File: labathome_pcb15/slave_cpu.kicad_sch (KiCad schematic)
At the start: 47 parts, among them J1 HALL, J26 STDC14, J27 ADDA, J28 Brushless, J30 Servo4, J31 Servo1, J32 Servo2, J33 Servo3, J34 STM32 EXT, U16 LM358, U3 DRV8313, U5 STM32G431R8Tx

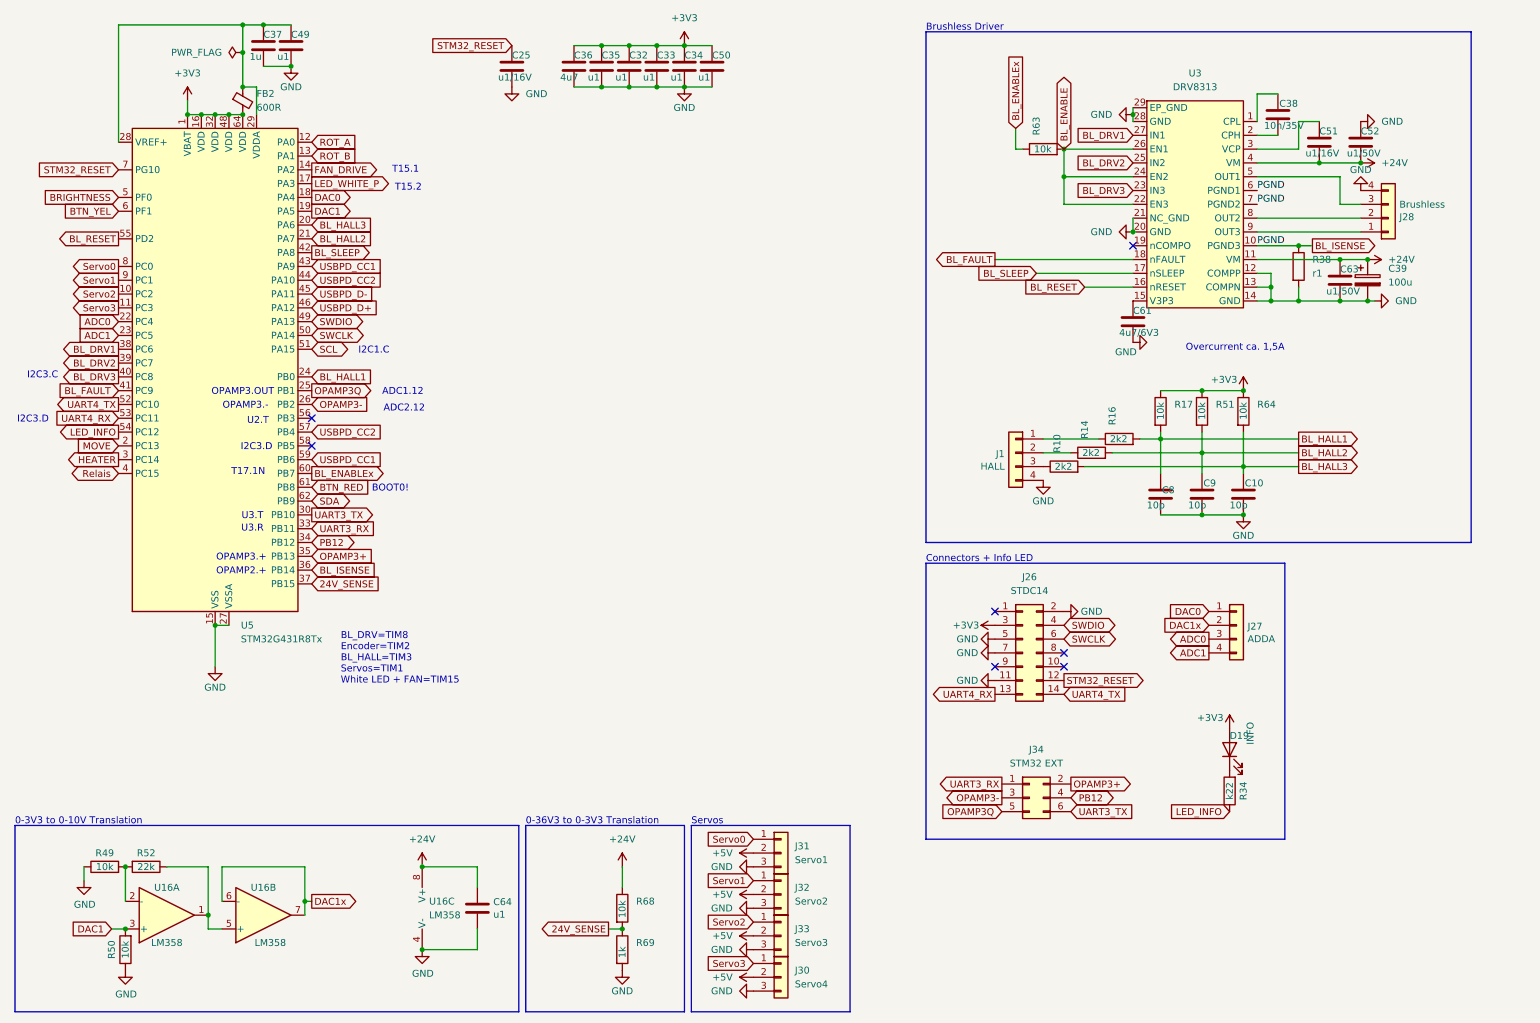
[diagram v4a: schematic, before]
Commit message: Reverse mount LEDs, switch
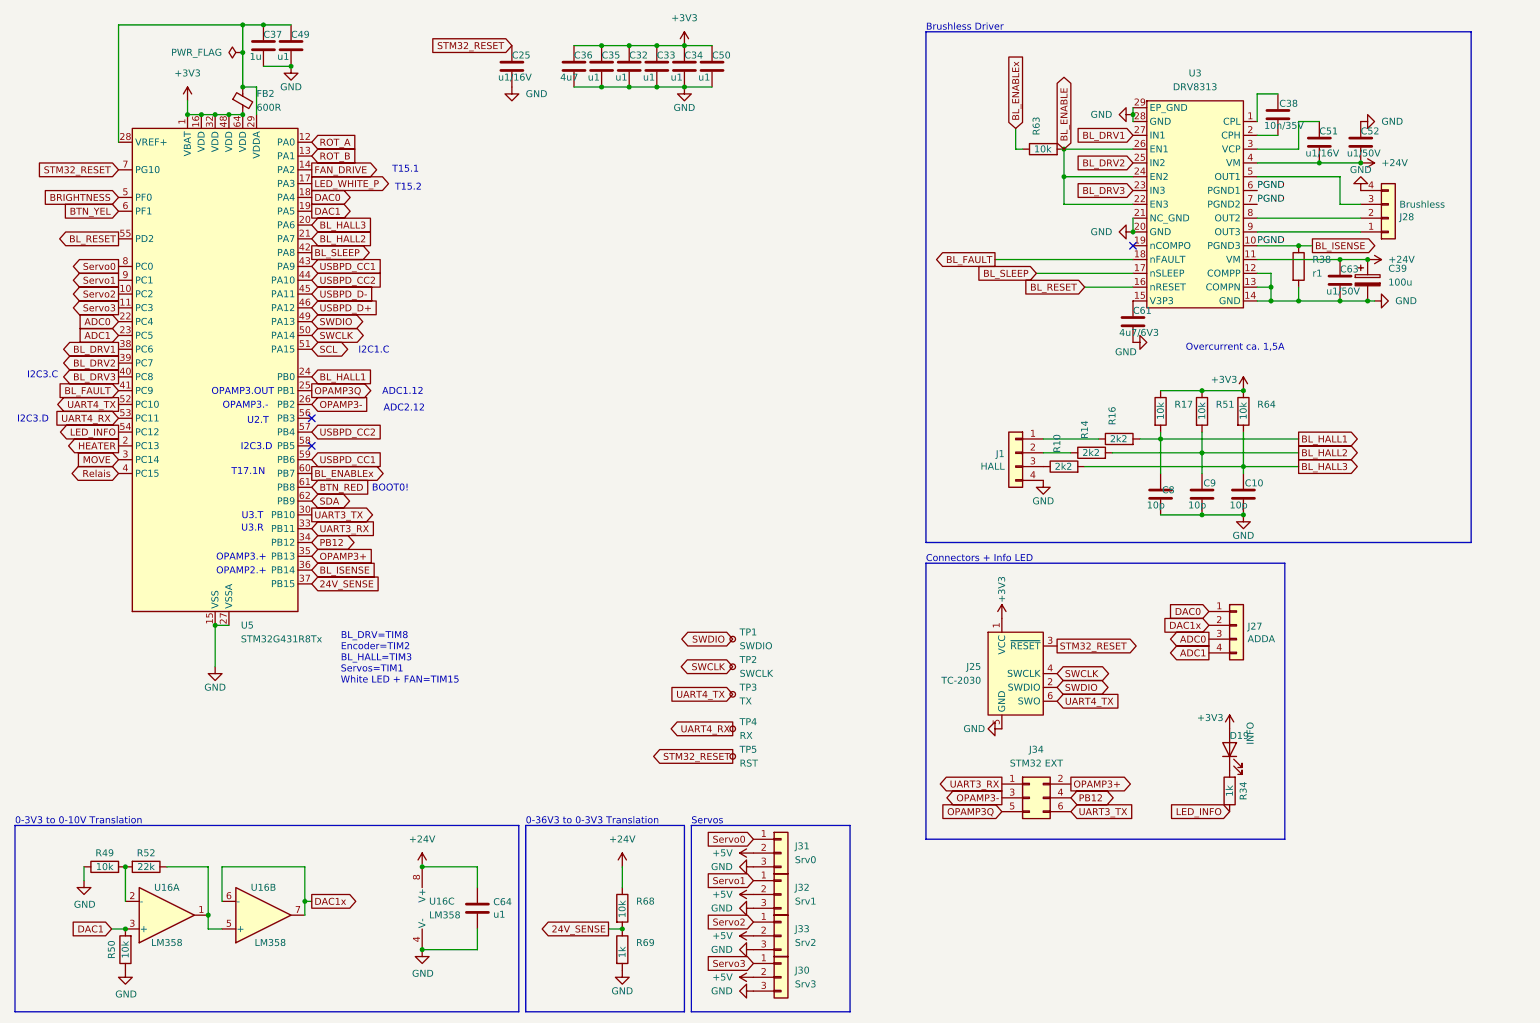
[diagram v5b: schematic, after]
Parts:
- removed J26: STDC14, Connector_IDC:IDC-Header_2x07_P2.54mm_Vertical, symbol Connector_Generic:Conn_02x07_Odd_Even
- added J25: TC-2030, Connector:Tag-Connect_TC2030-IDC-NL_2x03_P1.27mm_Vertical, symbol Connector:Conn_ARM_SWD_TagConnect_TC2030-NL
- added TP1: SWDIO, TestPoint:TestPoint_THTPad_D1.5mm_Drill0.7mm, symbol Connector:TestPoint_Small
- added TP2: SWCLK, TestPoint:TestPoint_THTPad_D1.5mm_Drill0.7mm, symbol Connector:TestPoint_Small
- added TP3: TX, TestPoint:TestPoint_THTPad_D1.5mm_Drill0.7mm, symbol Connector:TestPoint_Small
- added TP4: RX, TestPoint:TestPoint_THTPad_D1.5mm_Drill0.7mm, symbol Connector:TestPoint_Small
- added TP5: RST, TestPoint:TestPoint_THTPad_D1.5mm_Drill0.7mm, symbol Connector:TestPoint_Small
- D19: footprint LED_SMD:LED_0805_2012Metric_Pad1.15x1.40mm_HandSolder -> liebler_OPTO:LED_1206_3216Metric_ReverseMount
- J30: value Servo4 -> Srv3
- J31: value Servo1 -> Srv0
- J32: value Servo2 -> Srv1
- J33: value Servo3 -> Srv2
- R34: value k22 -> 1k
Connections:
- net +3V3: now also J25.1 (VCC)
- net GND: now also J25.5 (GND)
- net HEATER: now also U5.2 (PC13); no longer U5.3 (PC14)
- net MOVE: now also U5.3 (PC14); no longer U5.2 (PC13)
- net STM32_RESET: now also J25.3 (~{RESET}), TP5.1
- net SWCLK: now also J25.4 (SWCLK), TP2.1
- net SWDIO: now also J25.2 (SWDIO), TP1.1
- net UART4_RX: now also TP4.1
- net UART4_TX: now also J25.6 (SWO), TP3.1
- no-connect marks 7 -> 3

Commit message: Various last minute
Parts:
- removed TP2: SWCLK, TestPoint:TestPoint_THTPad_D1.5mm_Drill0.7mm, symbol Connector:TestPoint_Small
- removed TP3: TX, TestPoint:TestPoint_THTPad_D1.5mm_Drill0.7mm, symbol Connector:TestPoint_Small
- removed TP4: RX, TestPoint:TestPoint_THTPad_D1.5mm_Drill0.7mm, symbol Connector:TestPoint_Small
- removed TP5: RST, TestPoint:TestPoint_THTPad_D1.5mm_Drill0.7mm, symbol Connector:TestPoint_Small
- added J26: PROG STM, liebler_CONN:IDC_2x03_P1.27mm_Vertical, symbol Connector_Generic:Conn_02x03_Odd_Even
- C25: value u1/16V -> u1; footprint Capacitor_SMD:C_0402_1005Metric -> Capacitor_SMD:C_0201_0603Metric
- C32, C33, C34, C35, C49, C50: footprint Capacitor_SMD:C_0402_1005Metric -> Capacitor_SMD:C_0201_0603Metric
- C64: value u1 -> u1/24V
- J25: now not fitted
- R17, R50, R51, R63, R64, R68: footprint Resistor_SMD:R_0402_1005Metric -> Resistor_SMD:R_0201_0603Metric
- TP1: value SWDIO -> RX
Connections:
- net +3V3: now also J26.1 (Pin_1)
- net GND: now also J26.5 (Pin_5)
- net STM32_RESET: now also J26.3 (Pin_3)
- net SWCLK: now also J26.4 (Pin_4)
- net SWDIO: now also J26.2 (Pin_2); no longer TP1.1
- net UART4_RX: now also TP1.1
- net UART4_TX: now also J26.6 (Pin_6)

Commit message: PCB update IP5306 I2C
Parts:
- J26: footprint liebler_CONN:IDC_2x03_P1.27mm_Vertical -> liebler_CONN:PinHeader_2x03_P1.27mm_Vertical_SMD_handsolder
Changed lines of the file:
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@@
 			)
 		)
-		(property "Footprint" "liebler_CONN:IDC_2x03_P1.27mm_Vertical"
+		(property "Footprint" "liebler_CONN:PinHeader_2x03_P1.27mm_Vertical_SMD_handsolder"
 			(at 149.86 110.49 0)
 			(effects

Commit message: 4 Layers
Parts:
- C51: footprint Capacitor_SMD:C_0402_1005Metric -> Capacitor_SMD:C_0603_1608Metric
- C52, C63: value u1/50V -> u1/35V
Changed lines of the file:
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@@
 			)
 		)
-		(property "Value" "u1/50V"
+		(property "Value" "u1/35V"
 			(at 259.08 38.862 0)
 			(effects
@@
 			)
 		)
-		(property "Footprint" "Capacitor_SMD:C_0402_1005Metric"
+		(property "Footprint" "Capacitor_SMD:C_0603_1608Metric"
 			(at 254.9652 40.64 0)
 			(effects
@@
 			)
 		)
-		(property "Value" "u1/50V"
+		(property "Value" "u1/35V"
 			(at 255.27 64.262 0)
 			(effects
